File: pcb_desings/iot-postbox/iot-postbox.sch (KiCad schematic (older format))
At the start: 39 parts, among them J1 Switch_1, J2 Switch_2, J3 PowerIn, J4 USB_B_Micro, J5 Battery, J6 Battery, SW1 POWER, U1 ESP-12F, U2 TTL_UART_adapter_iot_postbox, U3 TP4056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

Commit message: Updated iot-postbox sch and pcb to v0.2 correcting Switch references
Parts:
- J1: renamed from J2; value Switch_2 -> Switch_1
- J2: renamed from J1; value Switch_1 -> Switch_2
- renumbered R7 to R6, R6 to R7
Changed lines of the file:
@@
 Title "IoT-PostBox"
 Date "2021-07-08"
-Rev "v0.1"
+Rev "v0.2"
 Comp ""
 Comment1 "https://github.com/paclema/iot-postbox"
@@
 Wire Wire Line
 	4200 6550 4700 6550
-Text Label 4550 6550 2    50   ~ 0
-GPIO13
-$Comp
-L Device:R R6
+$Comp
+L Device:R R7
 U 1 1 60B3CBFB
 P 4700 6850
-F 0 "R6" H 4770 6896 50  0000 L CNN
+F 0 "R7" H 4770 6896 50  0000 L CNN
 F 1 "10K" H 4770 6805 50  0000 L CNN
 F 2 "Resistor_SMD:R_0805_2012Metric" V 4630 6850 50  0001 C CNN
@@
 GPIO12
 $Comp
-L Device:R R7
+L Device:R R6
 U 1 1 60B42581
 P 5800 6850
-F 0 "R7" H 5870 6896 50  0000 L CNN
+F 0 "R6" H 5870 6896 50  0000 L CNN
 F 1 "10K" H 5870 6805 50  0000 L CNN
 F 2 "Resistor_SMD:R_0805_2012Metric" V 5730 6850 50  0001 C CNN
@@
 OUT
 $Comp
-L Connector_Generic:Conn_01x02 J2
-U 1 1 60B5CB01
-P 6000 6250
-F 0 "J2" H 6080 6242 50  0000 L CNN
-F 1 "Switch_2" H 6080 6151 50  0000 L CNN
-F 2 "Connector_PinHeader_2.54mm:PinHeader_1x02_P2.54mm_Vertical" H 6000 6250 50  0001 C CNN
-F 3 "~" H 6000 6250 50  0001 C CNN
-	1    6000 6250
-	1    0    0    -1
-$EndComp
-$Comp
-L Connector_Generic:Conn_01x02 J1
-U 1 1 60B69ADF
-P 4900 6250
-F 0 "J1" H 4980 6242 50  0000 L CNN
-F 1 "Switch_1" H 4980 6151 50  0000 L CNN
-F 2 "Connector_PinHeader_2.54mm:PinHeader_1x02_P2.54mm_Vertical" H 4900 6250 50  0001 C CNN
-F 3 "~" H 4900 6250 50  0001 C CNN
-	1    4900 6250
-	1    0    0    -1
-$EndComp
-$Comp
 L ttl_to_usb_adapter:TTL_UART_adapter_iot_postbox U2
 U 1 1 60E75D33
@@
 Text Notes 700  1250 0    50   ~ 0
 For ESP-07s pull-ups/down resistors are not required for RST,\nGPIO0, GPIO2 and GPIO15
+$Comp
+L Connector_Generic:Conn_01x02 J1
+U 1 1 60B5CB01
+P 6000 6250
+F 0 "J1" H 6080 6242 50  0000 L CNN
+F 1 "Switch_1" H 6080 6151 50  0000 L CNN
+F 2 "Connector_PinHeader_2.54mm:PinHeader_1x02_P2.54mm_Vertical" H 6000 6250 50  0001 C CNN
+F 3 "~" H 6000 6250 50  0001 C CNN
+	1    6000 6250
+	1    0    0    -1
+$EndComp
+$Comp
+L Connector_Generic:Conn_01x02 J2
+U 1 1 60B69ADF
+P 4900 6250
+F 0 "J2" H 4980 6242 50  0000 L CNN
+F 1 "Switch_2" H 4980 6151 50  0000 L CNN
+F 2 "Connector_PinHeader_2.54mm:PinHeader_1x02_P2.54mm_Vertical" H 4900 6250 50  0001 C CNN
+F 3 "~" H 4900 6250 50  0001 C CNN
+	1    4900 6250
+	1    0    0    -1
+$EndComp
+Text Label 4550 6550 2    50   ~ 0
+GPIO13
 $EndSCHEMATC

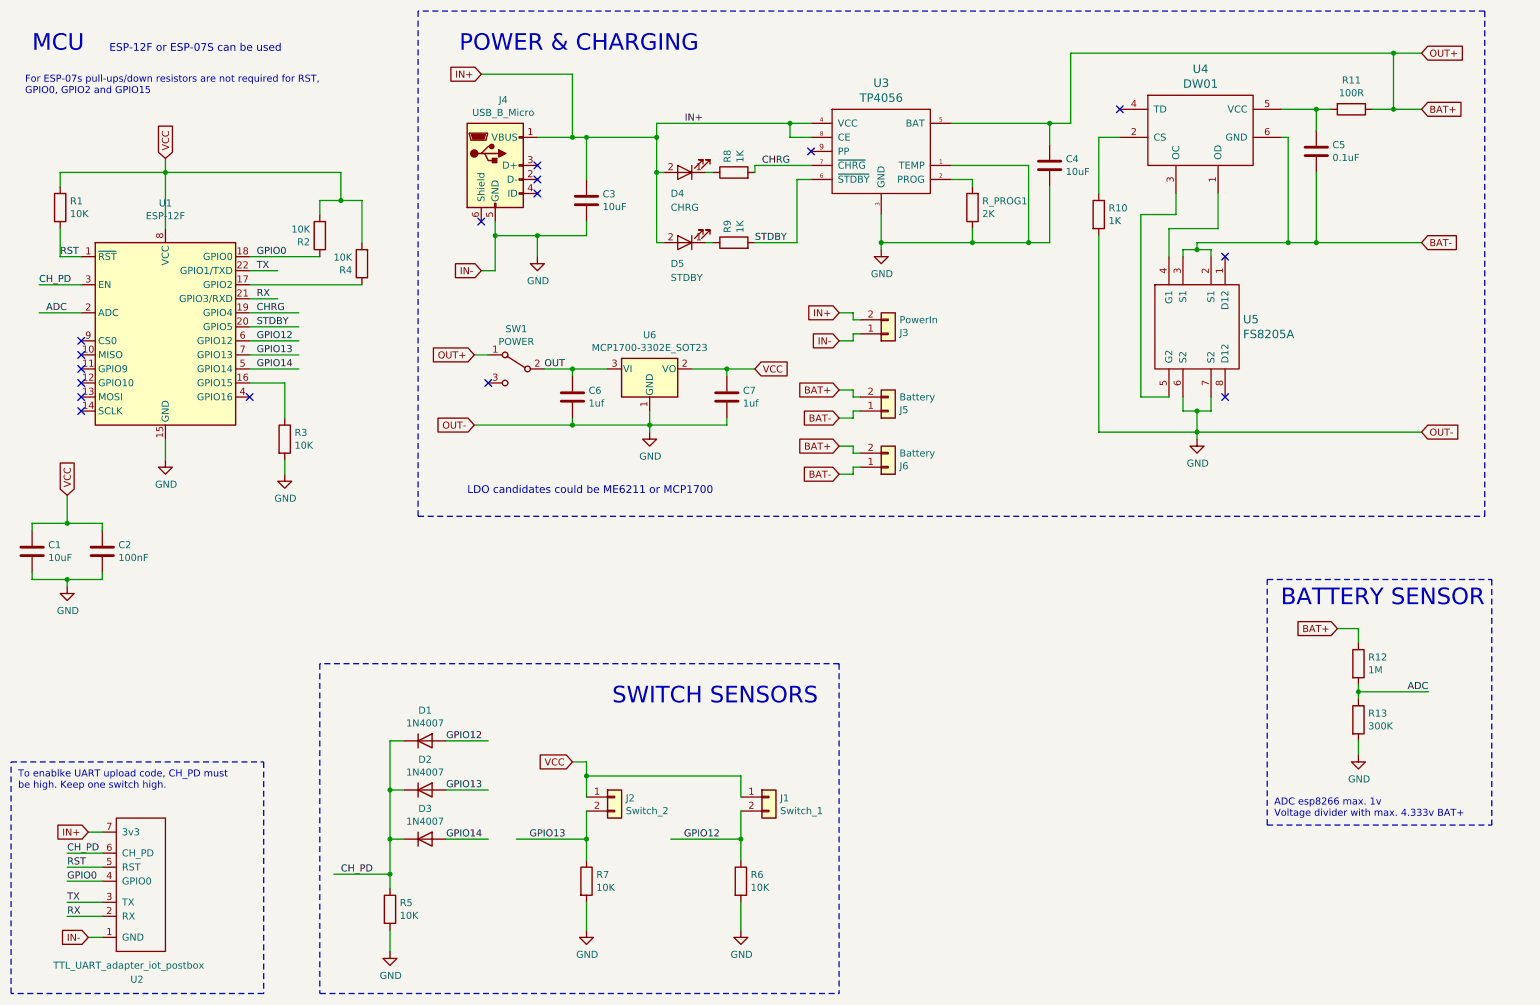
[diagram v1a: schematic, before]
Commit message: Exported pcb iot-postbox v0.3. Added ws2812b led strip to sch and pcb
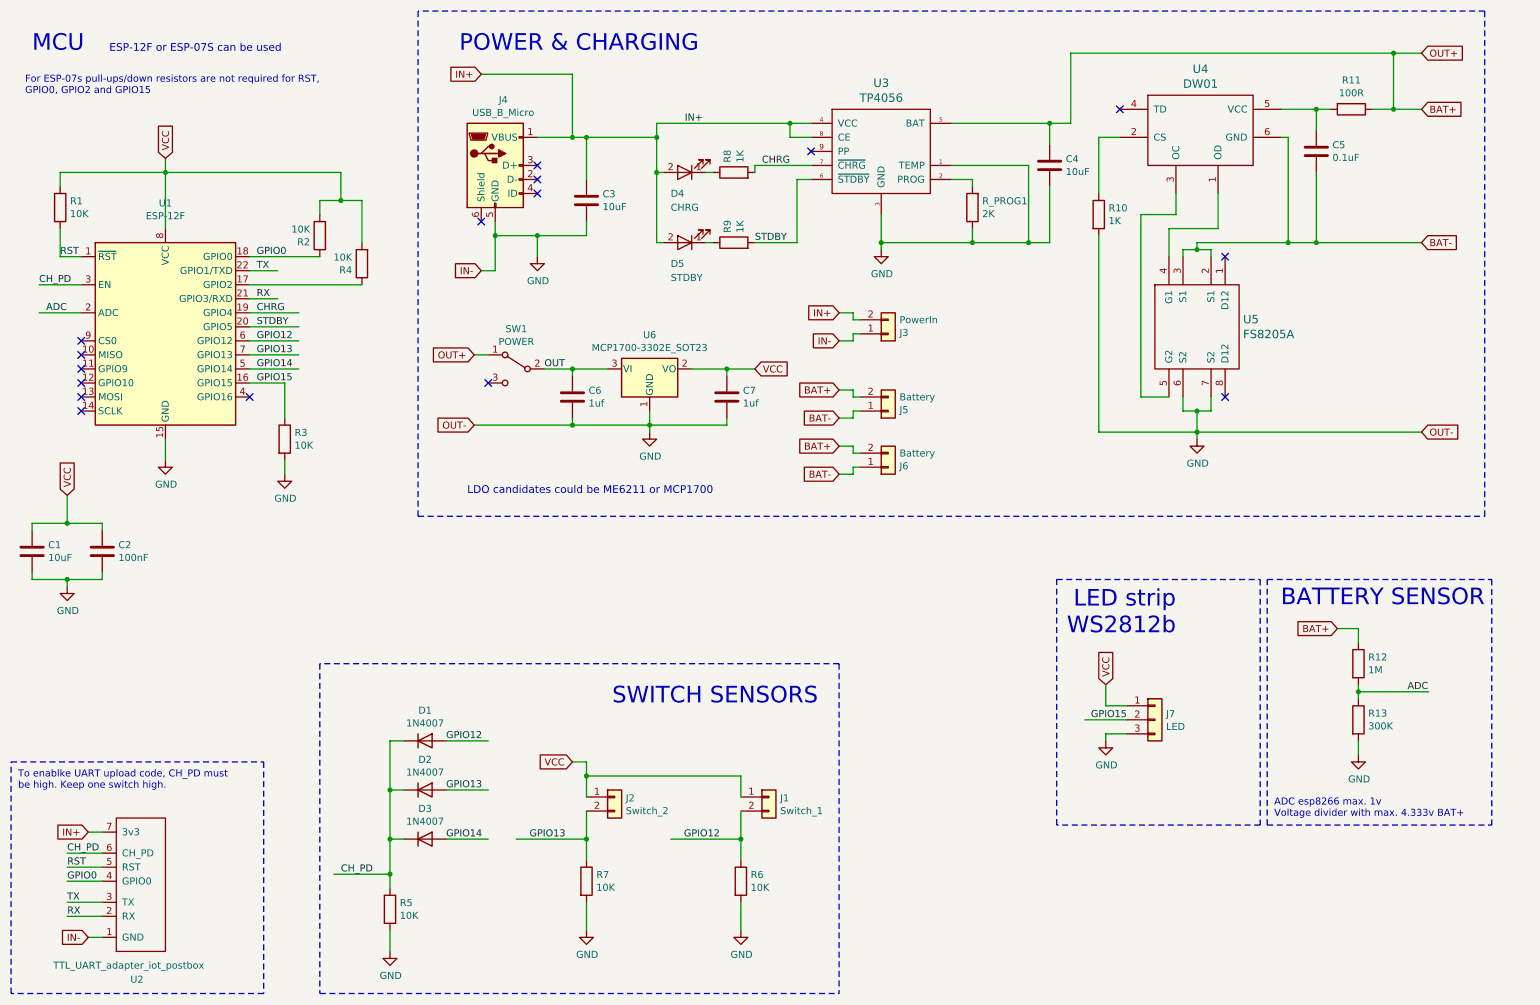
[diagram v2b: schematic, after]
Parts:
- added J7: LED, Connector_PinHeader_2.54mm:PinHeader_1x03_P2.54mm_Vertical, symbol Connector_Generic:Conn_01x03
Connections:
- net labels added: GPIO15
- wire segments 188 -> 193
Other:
- note added: "LED strip\nWS2812b"
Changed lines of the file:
@@
 Title "IoT-PostBox"
 Date "2021-07-08"
-Rev "v0.2"
+Rev "v0.3"
 Comp ""
 Comment1 "https://github.com/paclema/iot-postbox"
@@
 Text Label 4550 6550 2    50   ~ 0
 GPIO13
+$Comp
+L Connector_Generic:Conn_01x03 J7
+U 1 1 61C271A5
+P 8750 5700
+F 0 "J7" H 8830 5742 50  0000 L CNN
+F 1 "LED" H 8830 5651 50  0000 L CNN
+F 2 "Connector_PinHeader_2.54mm:PinHeader_1x03_P2.54mm_Vertical" H 8750 5700 50  0001 C CNN
+F 3 "~" H 8750 5700 50  0001 C CNN
+	1    8750 5700
+	1    0    0    -1
+$EndComp
+Text Label 2350 3300 0    50   ~ 0
+GPIO15
+Text Label 8550 5700 2    50   ~ 0
+GPIO15
+Text GLabel 8400 5450 1    50   Input ~ 0
+VCC
+$Comp
+L power:GND #PWR05
+U 1 1 61C4413E
+P 8400 5850
+F 0 "#PWR05" H 8400 5600 50  0001 C CNN
+F 1 "GND" H 8405 5677 50  0000 C CNN
+F 2 "" H 8400 5850 50  0001 C CNN
+F 3 "" H 8400 5850 50  0001 C CNN
+	1    8400 5850
+	1    0    0    -1
+$EndComp
+Wire Wire Line
+	8550 5800 8400 5800
+Wire Wire Line
+	8400 5800 8400 5850
+Wire Wire Line
+	8550 5700 8250 5700
+Wire Wire Line
+	8550 5600 8400 5600
+Wire Wire Line
+	8400 5600 8400 5450
+Wire Notes Line
+	9500 6450 8050 6450
+Wire Notes Line
+	8050 6450 8050 4700
+Wire Notes Line
+	8050 4700 9500 4700
+Wire Notes Line
+	9500 4700 9500 6450
+Text Notes 8900 5100 2    118  ~ 0
+LED strip\nWS2812b
 $EndSCHEMATC
